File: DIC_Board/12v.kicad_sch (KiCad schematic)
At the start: 32 parts, among them Q100 CSD18542KTTT, Q101 CSD18542KTTT, U10 TPS552882RPMR

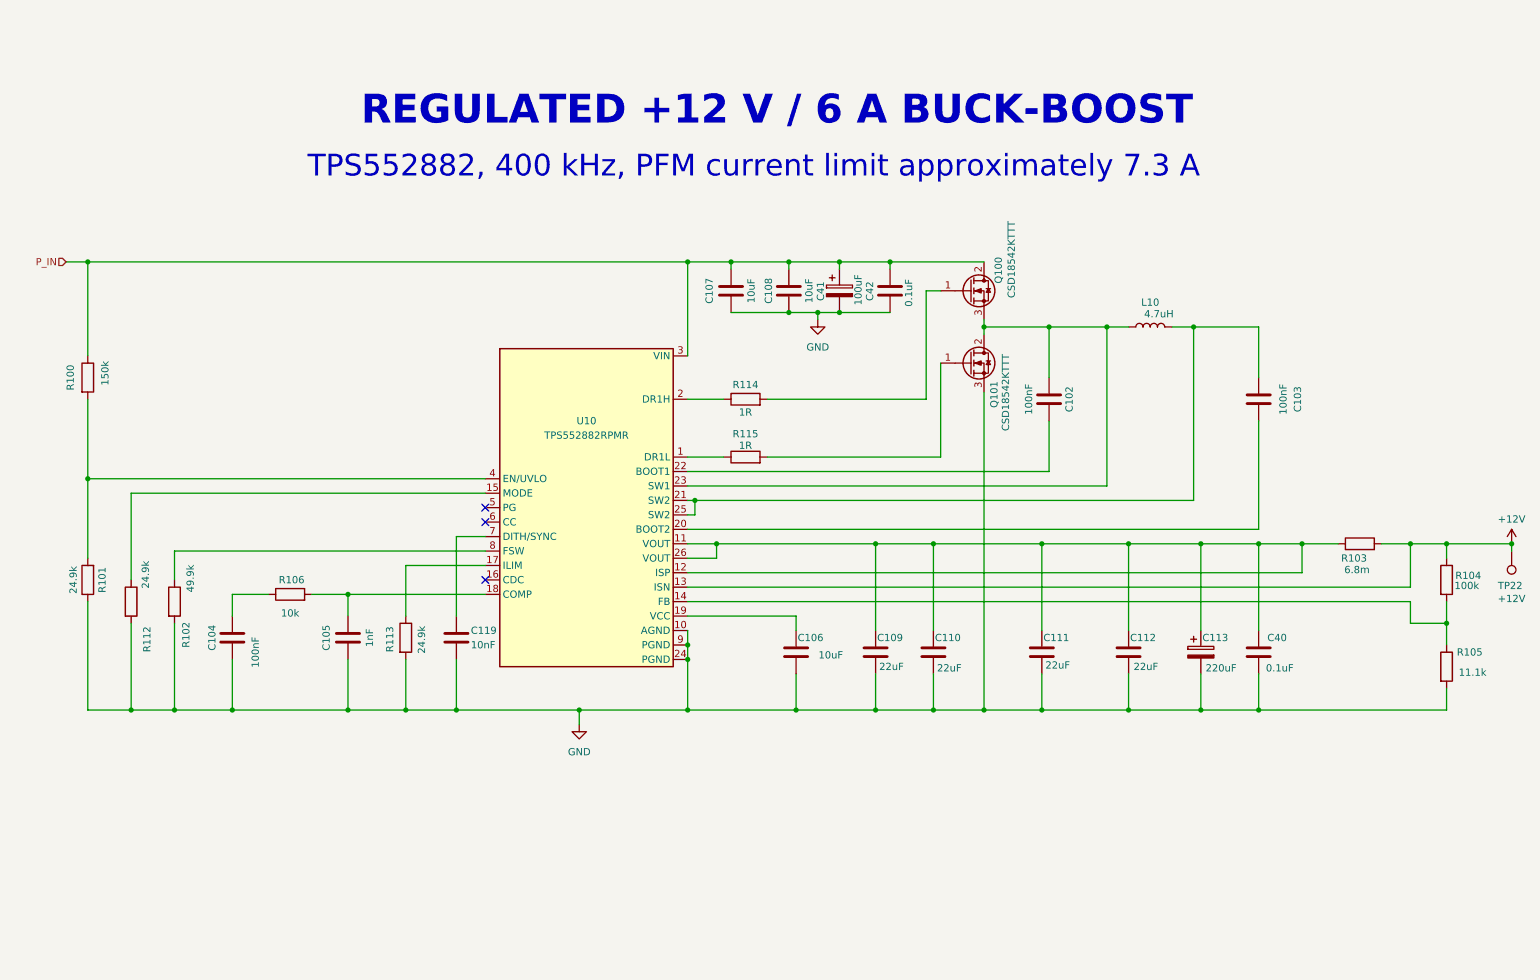
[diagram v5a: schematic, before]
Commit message: Changed the 12V regulator to an integrated IC
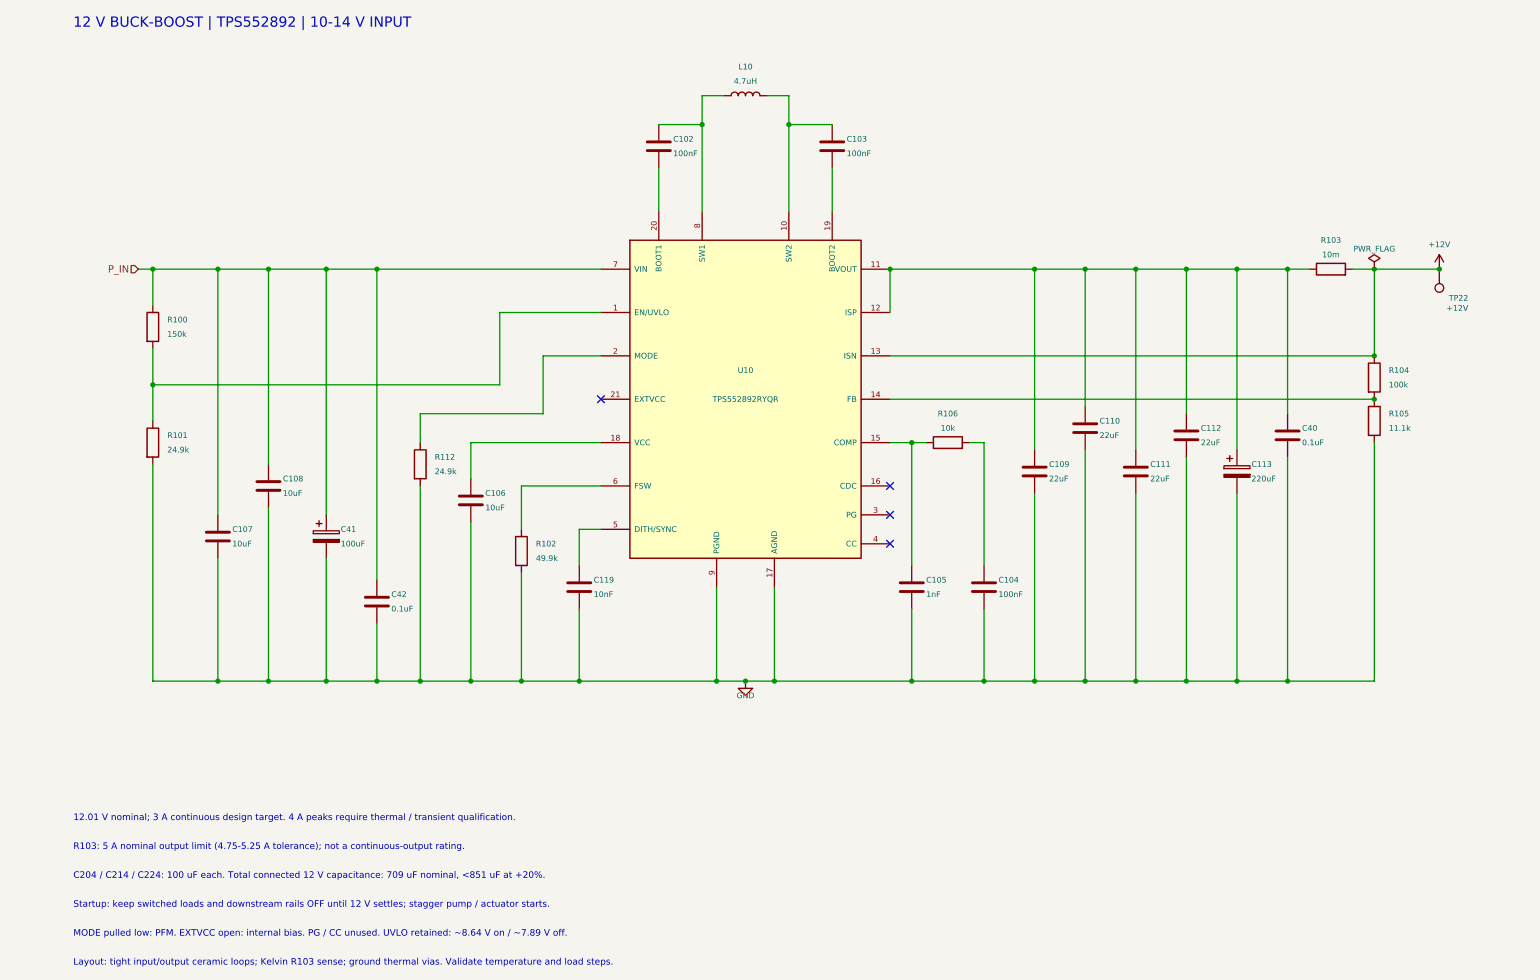
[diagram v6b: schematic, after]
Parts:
- removed Q100, Q101: CSD18542KTTT, Package_TO_SOT_SMD:TO-263-3_TabPin2, symbol Transistor_FET:Q_NMOS_GDS
- removed R113: 24.9k, Resistor_SMD:R_0402_1005Metric, symbol Device:R
- removed R114, R115: 1R, Resistor_SMD:R_0603_1608Metric, symbol Device:R
- R103: value 6.8m -> 10m; MPN WSL25126L800FEA -> WSL2512R0100FEA; Source (none) -> https://www.vishay.com/docs/30100/wsl.pdf
- U10: value TPS552882RPMR -> TPS552892RYQR; footprint DIC_Board:Texas_RPM0026A_TPS552882 -> DIC_Board:Texas_RYQ0021A_TPS552892; symbol DIC_Board:TPS552882 -> DIC_Board:TPS552892; BOM Comments (none) -> RYQ0021A, 21 pins; all four MOSFETs internal; not pin compa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; MPN TPS552882RPMR -> TPS552892RYQR; Source (none) -> https://www.ti.com/product/TPS552892
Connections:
- net GND: now also R101.2, U10.17 (AGND); no longer R101.1, U10.10 (AGND), U10.24 (PGND)
- net P_IN: now also U10.7 (VIN); no longer U10.3 (VIN)
- net at C109.1, C110.1, C111.1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: no longer U10.26 (VOUT)
- net at R102.1: now also U10.6 (FSW); no longer U10.8 (FSW)
- net at R106.1: now also C105.1, U10.15 (COMP); no longer C104.1
- net at C103.1: now also L10.2, U10.10 (SW2); no longer U10.20 (BOOT2)
- net at C102.1, L10.1: now also U10.8 (SW1); no longer U10.23 (SW1)
- net at U10.1 (EN/UVLO): now also R100.2, R101.1
- net at C102.2: now also U10.20 (BOOT1); no longer U10.22 (BOOT1)
- net at R112.1: now also U10.2 (MODE); no longer U10.15 (MODE)
- net at U10.19 (BOOT2): now also C103.2; no longer C106.1
- net at U10.5 (DITH/SYNC): now also C119.1
- new net: C104.1, R106.2
- new net: C106.1, U10.18 (VCC)
- now unconnected: U10.21 (SW2), U10.4 (EN/UVLO)
- no-connect marks 3 -> 4
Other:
- note added: "12 V BUCK-BOOST | TPS552892 | 10-14 V INPUT"
- note added: "12.01 V nominal; 3 A continuous design target. 4 A peaks require thermal / transient qualification."
- note added: "C204 / C214 / C224: 100 uF each. Total connected 12 V capacitance: 709 uF nominal, <851 uF at +20%."
- note added: "Layout: tight input/output ceramic loops; Kelvin R103 sense; ground thermal vias. Validate temperature and load steps."
- note added: "MODE pulled low: PFM. EXTVCC open: internal bias. PG / CC unused. UVLO retained: ~8.64 V on / ~7.89 V off."
- note added: "R103: 5 A nominal output limit (4.75-5.25 A tolerance); not a continuous-output rating."
- note added: "Startup: keep switched loads and downstream rails OFF until 12 V settles; stagger pump / actuator starts."
- note removed: "REGULATED +12 V / 6 A BUCK-BOOST"
- note removed: "TPS552882, 400 kHz, PFM current limit approximately 7.3 A"
- moved on the sheet: C102, C103, C104, C105, C106, C107, C108, C109, C110, C111, C112, C113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

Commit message: resized the board to 9.5 in by 2 in
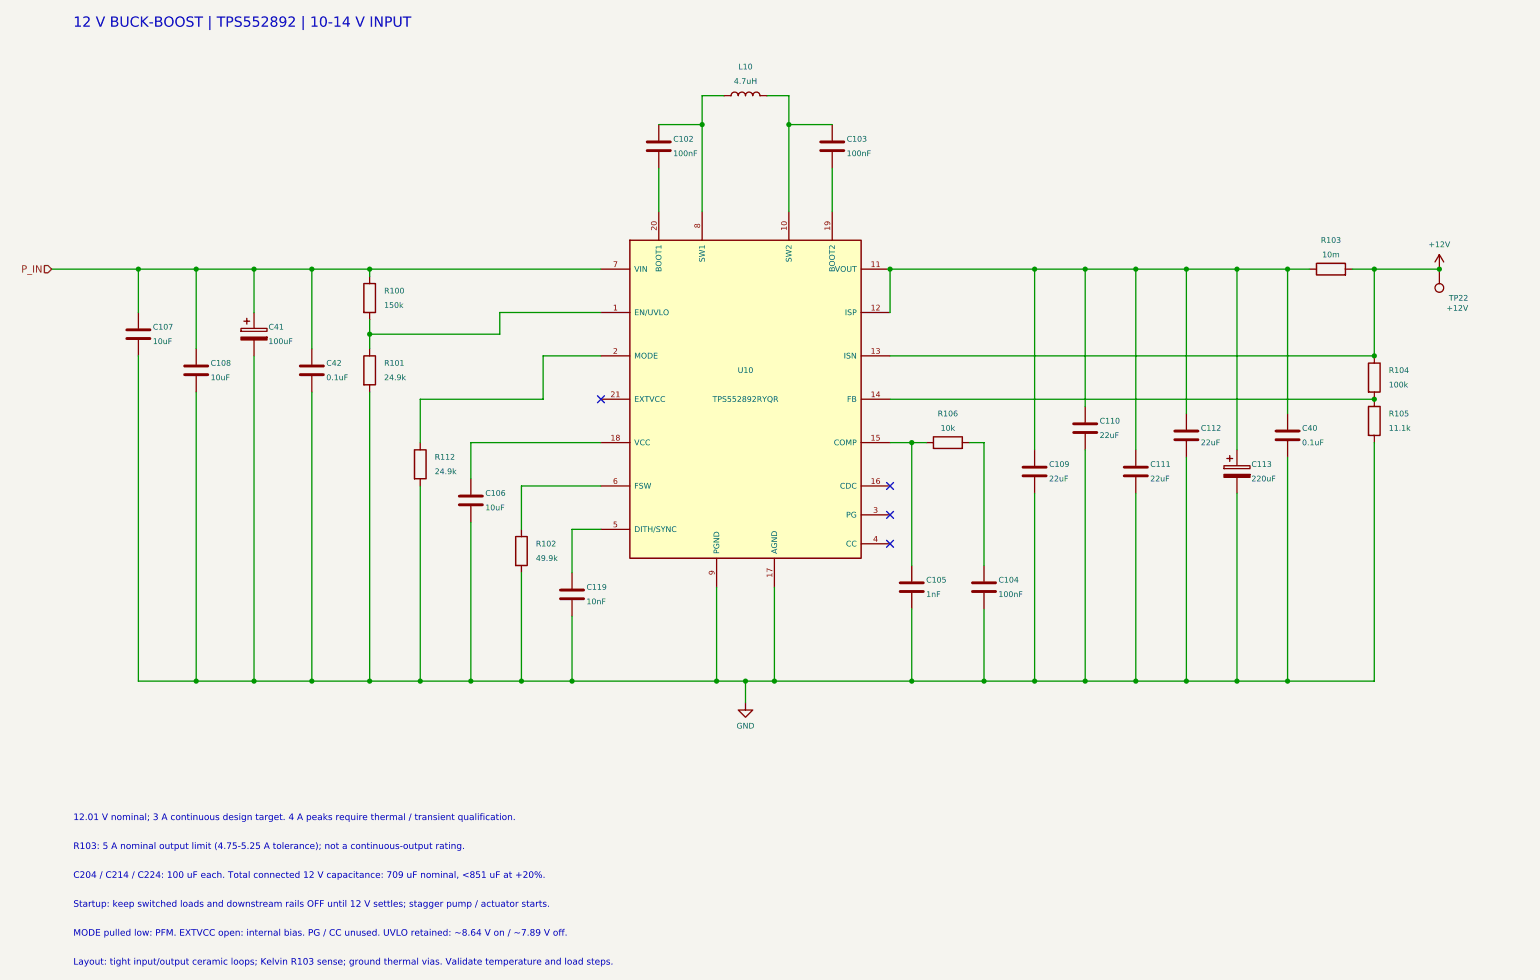
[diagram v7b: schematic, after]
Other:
- moved on the sheet: C107, C108, C119, C41, C42, R100, R101
